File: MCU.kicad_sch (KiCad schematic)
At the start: 52 parts, among them J6 USB_C_Receptacle_USB2.0_16P, Q7 SI2301BDS, SW1 TS2306A, U16 W25Q128JVPIQ, U17 RP2354A, U4 TPD2E001DRLR, Y4 40MHz

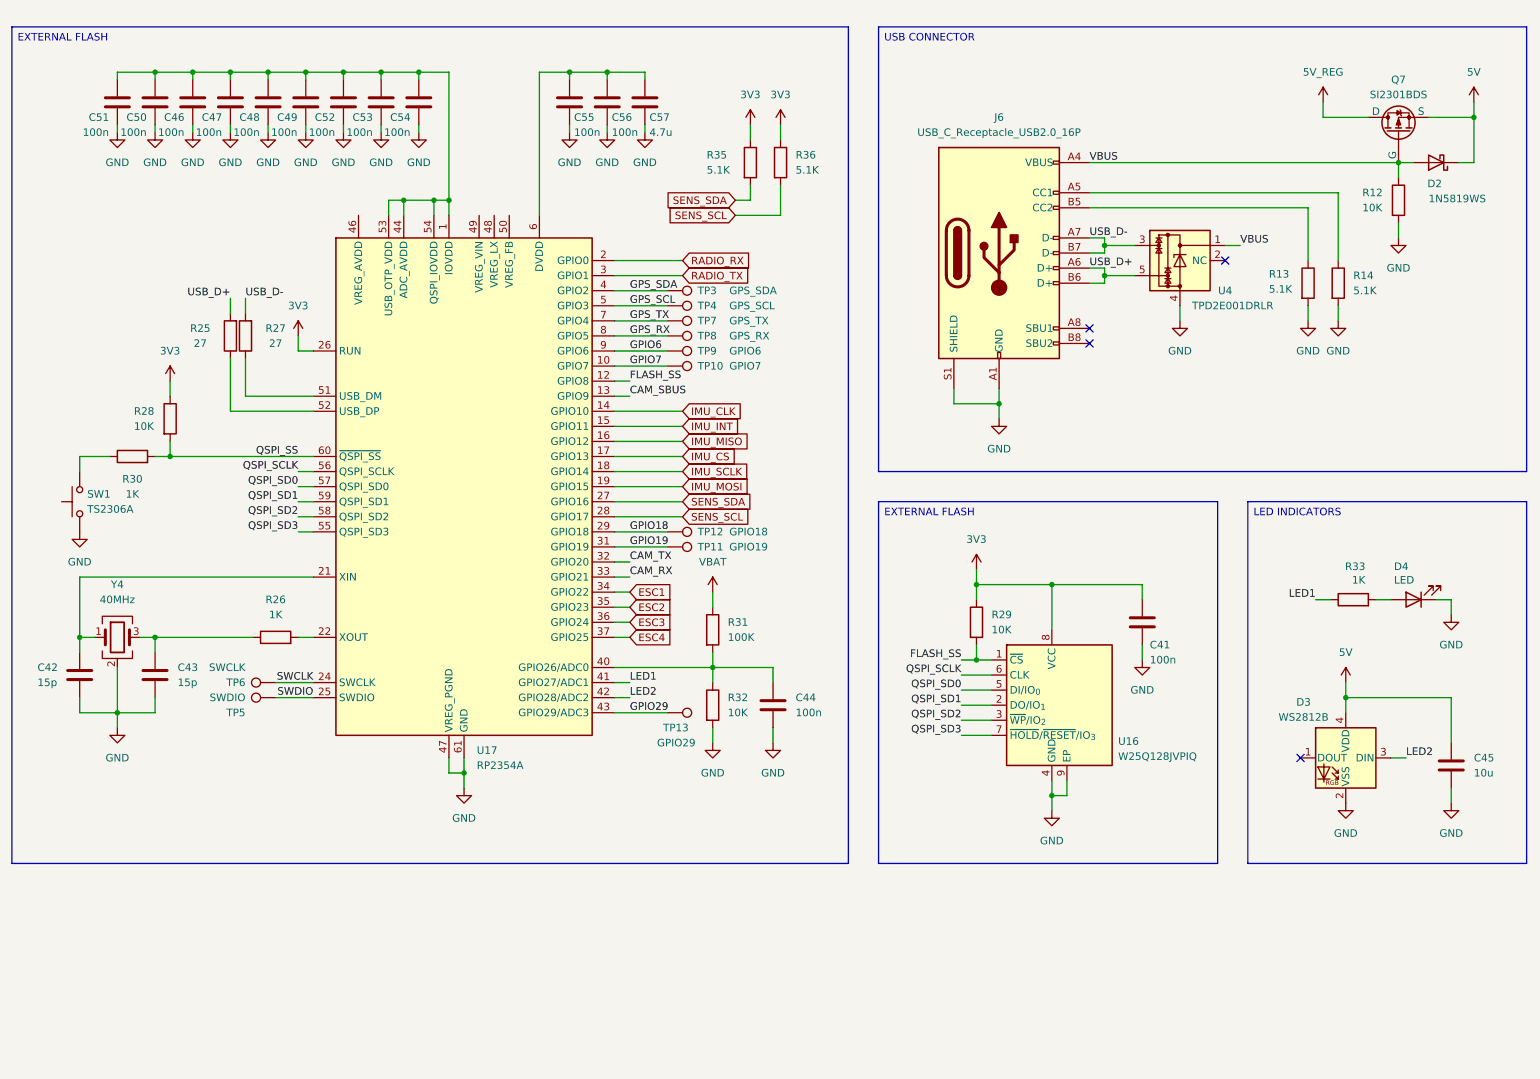
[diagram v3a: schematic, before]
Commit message: Complete ESC and MCU
Added the 4 ESC to the eschematic.
Updated the MCU design to add the connectors and buzzer.
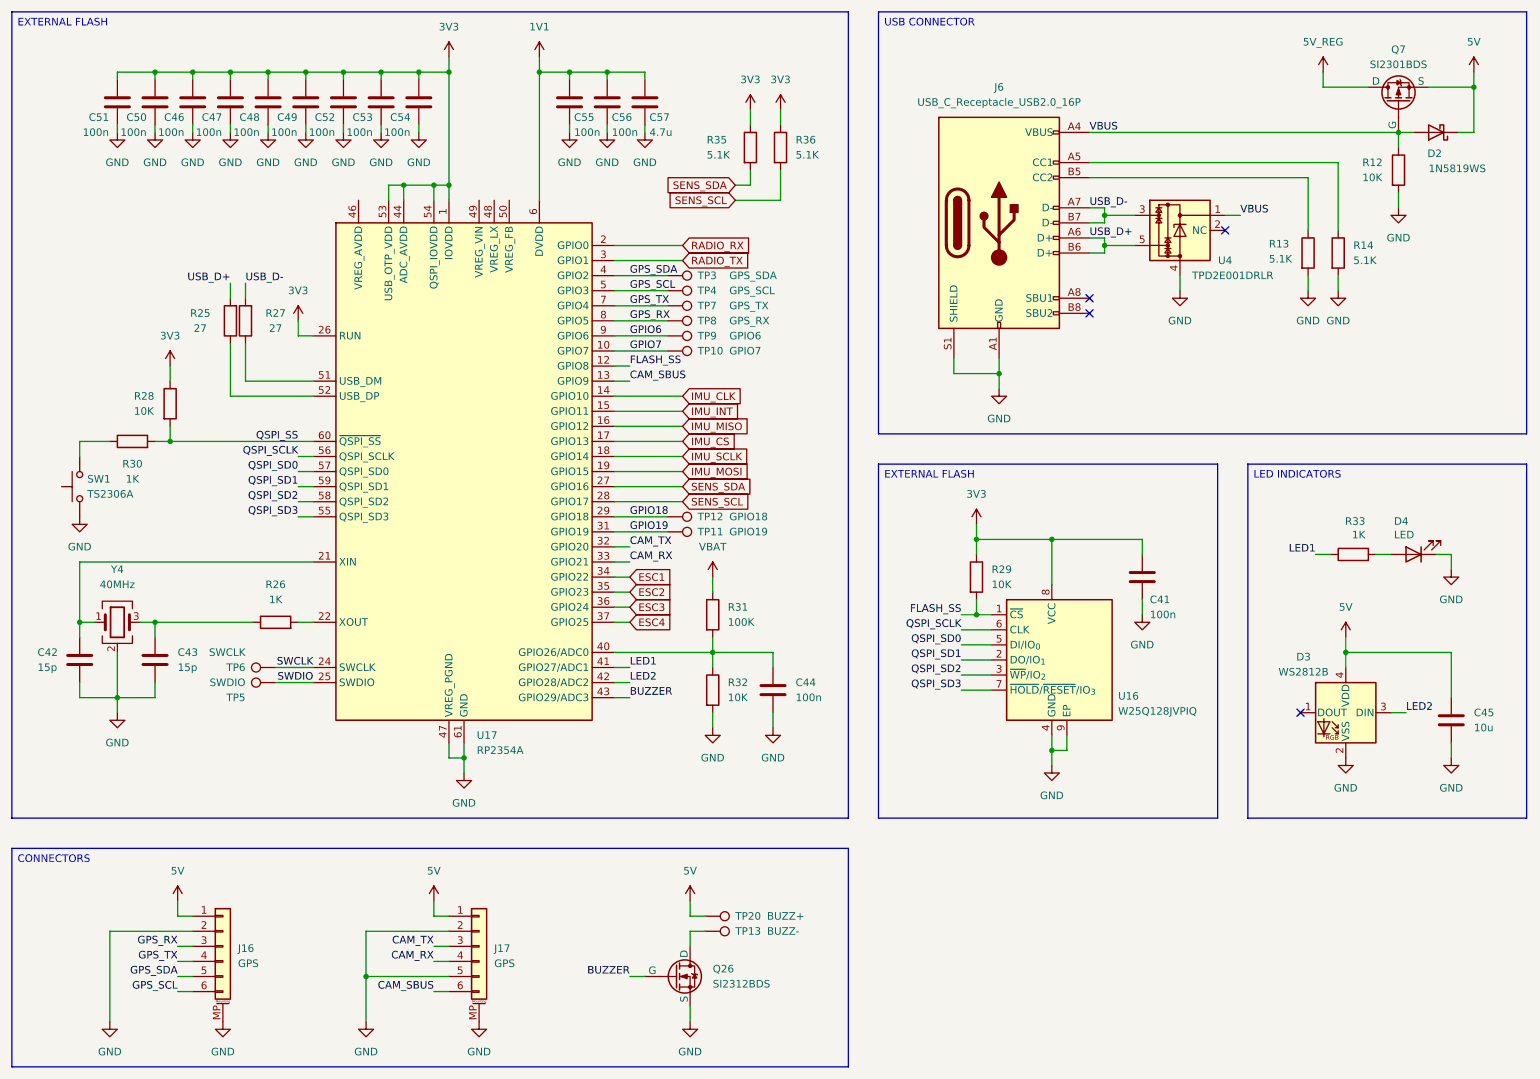
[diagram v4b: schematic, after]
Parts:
- added J16, J17: GPS, Connector_JST:JST_SH_SM06B-SRSS-TB_1x06-1MP_P1.00mm_Horizontal, symbol Connector_Generic_MountingPin:Conn_01x06_MountingPin
- added Q26: SI2312BDS, Package_TO_SOT_SMD:SOT-23, symbol Custom_Parts:SI2312BDS
- added TP20: BUZZ+, TestPoint:TestPoint_Pad_D1.0mm, symbol Connector:TestPoint
- TP13: value GPIO29 -> BUZZ-
- U17: footprint Package_DFN_QFN:QFN-60-1EP_7x7mm_P0.4mm_EP3.4x3.4mm -> Custom_Parts:RP2350A_QFN-60_EP_7.75x7.75_Pitch0.4mm
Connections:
- net 3V3: now also C46.1, C47.1, C48.1, C49.1, C50.1, C51.1, C52.1, C53.1, C54.1, U17.1 (IOVDD), U17.11 (IOVDD), U17.20 (IOVDD), U17.30 (IOVDD), U17.38 (IOVDD), U17.44 (ADC_AVDD), U17.45 (IOVDD), U17.53 (USB_OTP_VDD), U17.54 (QSPI_IOVDD)
- net 5V: now also J16.1 (Pin_1), J17.1 (Pin_1), TP20.1
- net CAM_RX: now also J17.4 (Pin_4)
- net CAM_SBUS: now also J17.6 (Pin_6)
- net CAM_TX: now also J17.3 (Pin_3)
- net GND: now also J16.2 (Pin_2), J16.MP (MountPin), J17.2 (Pin_2), J17.5 (Pin_5), J17.MP (MountPin), Q26.2 (S)
- net GPS_RX: now also J16.3 (Pin_3)
- net GPS_SCL: now also J16.6 (Pin_6)
- net GPS_SDA: now also J16.5 (Pin_5)
- net GPS_TX: now also J16.4 (Pin_4)
- net 1V1: now reaches C55.1, C56.1, C57.1, U17.23 (DVDD), U17.39 (DVDD), U17.6 (DVDD)
- net GPIO29: no longer names the net of TP13.1
- net GPIO29: now also Q26.3 (D); no longer U17.43 (GPIO29/ADC3)
- new net BUZZER: Q26.1 (G), U17.43 (GPIO29/ADC3)
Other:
- moved on the sheet: C41, C42, C43, C44, C45, D2, D3, D4, J6, Q7, R12, R13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

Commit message: Power design
Added the 5V regulator schematic.
Updated the MCU schematic.
Updated the RX schematic.
Updated the sensors schematic.

TODO:
Calculate the voltage divider for the 5V regulator.
Review all connections and systems.
Select the footprints for the missing components.
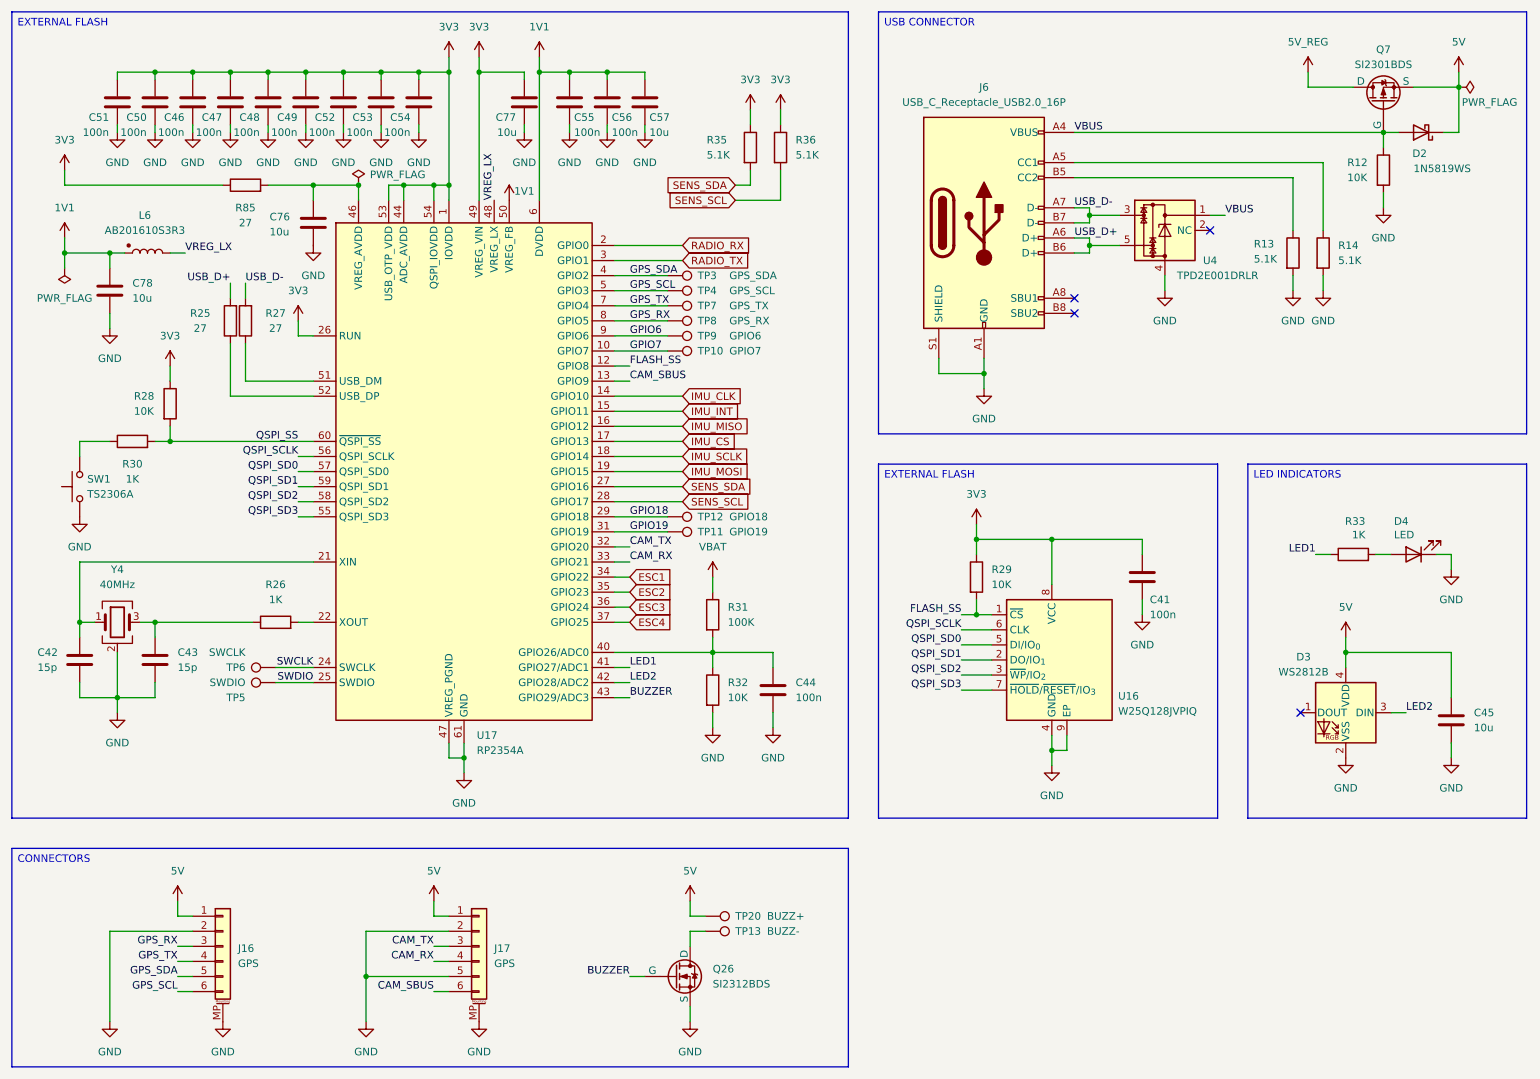
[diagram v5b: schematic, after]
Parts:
- added C76, C77, C78: 10u, symbol Device:C
- added L6: AB201610S3R3, symbol Custom_Parts:L_Polarized
- added R85: 27, symbol Device:R
- C57: value 4.7u -> 10u
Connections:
- net 1V1: now also U17.50 (VREG_FB), C78.1, L6.1
- net 3V3: now also U17.49 (VREG_VIN), C77.1, R85.1
- net GND: now also C76.2, C77.2, C78.2
- net at U17.46 (VREG_AVDD): now also C76.1, R85.2
- net VREG_LX: now reaches U17.48 (VREG_LX)
- net VREG_LX: now also L6.2
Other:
- moved on the sheet: D2, J6, Q7, R12, R13, R14, U4

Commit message: Footprints and revision
Added the missing footprints.
Updated a all the schematics.
Completed an initial review of the schematics.

TODO:
Perform a deep review of the schematics before committing to layout.
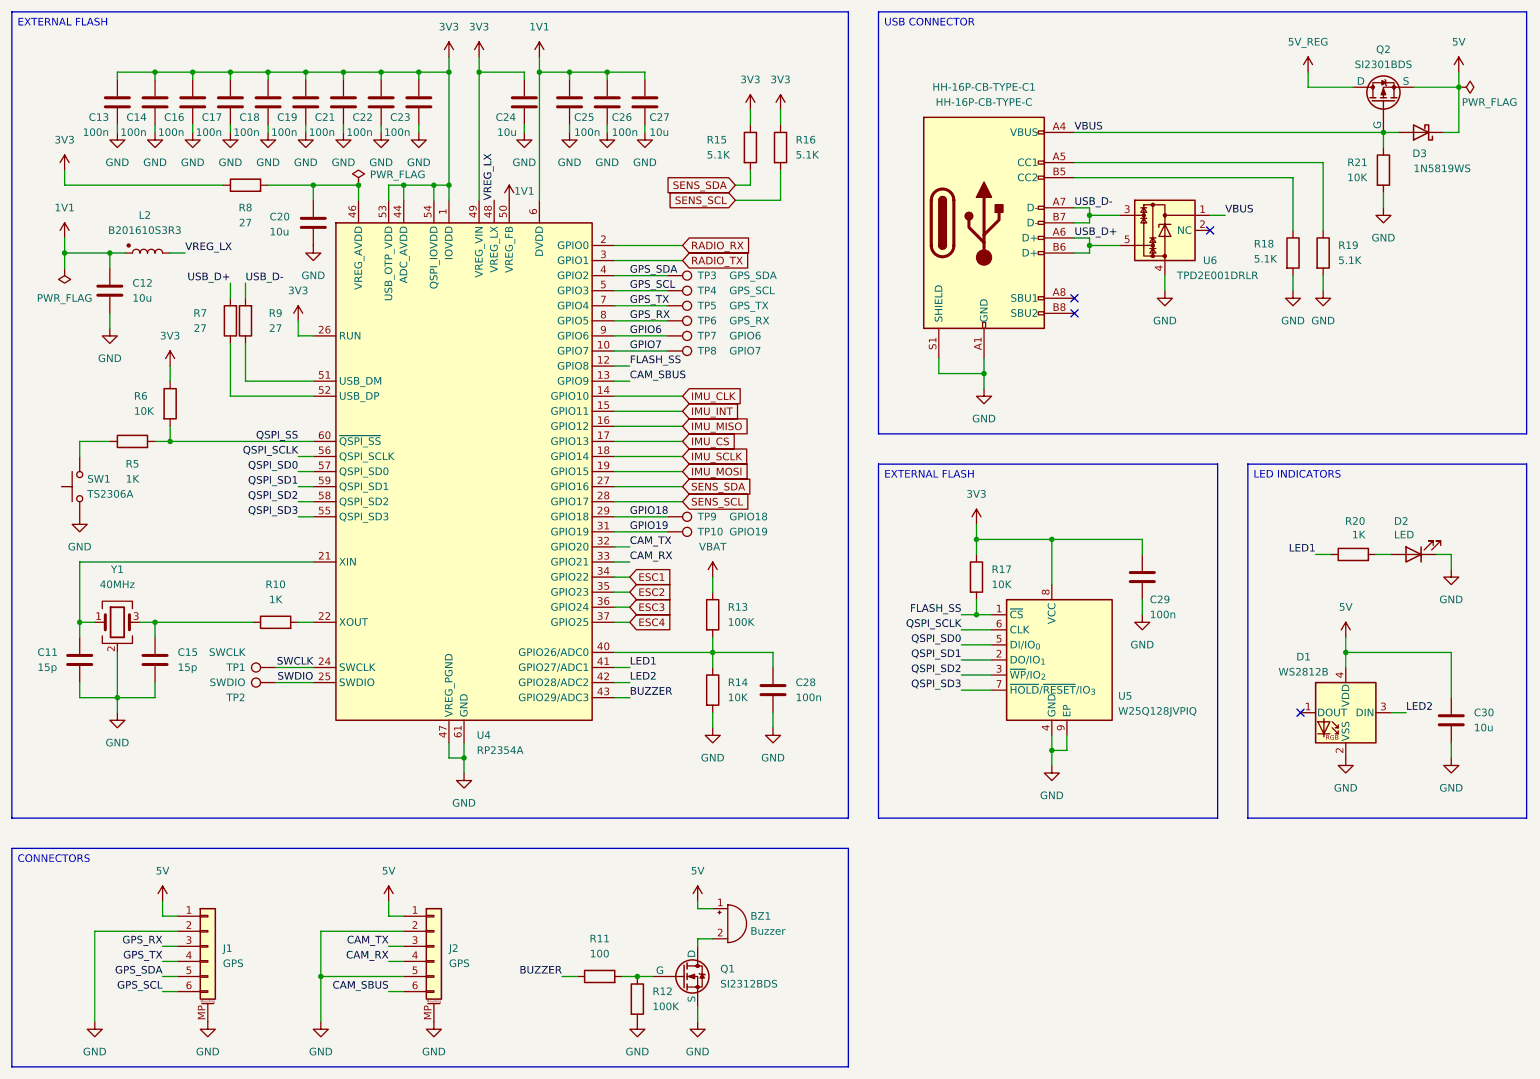
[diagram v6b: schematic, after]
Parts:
- removed J6: USB_C_Receptacle_USB2.0_16P, Custom_Parts:HH-16P-CB-TYPE-C, symbol Connector:USB_C_Receptacle_USB2.0_16P
- removed TP13: BUZZ-, TestPoint:TestPoint_Pad_D1.0mm, symbol Connector:TestPoint
- removed TP20: BUZZ+, TestPoint:TestPoint_Pad_D1.0mm, symbol Connector:TestPoint
- added BZ1: Buzzer, Custom_Parts:FUET_9018, symbol Device:Buzzer
- added HH-16P-CB-TYPE-C1: HH-16P-CB-TYPE-C, Custom_Parts:HH-16P-CB-TYPE-C, symbol Custom_Parts:HH-16P-CB-TYPE-C
- added R11: 100, Resistor_SMD:R_0603_1608Metric, symbol Device:R
- added R12: 100K, Resistor_SMD:R_0603_1608Metric, symbol Device:R
- C11: renamed from C42; footprint (none) -> Capacitor_SMD:C_0603_1608Metric
- C12: renamed from C78; footprint (none) -> Capacitor_SMD:C_0805_2012Metric
- C13: renamed from C51; footprint (none) -> Capacitor_SMD:C_0201_0603Metric
- C14: renamed from C50; footprint (none) -> Capacitor_SMD:C_0201_0603Metric
- C15: renamed from C43; footprint (none) -> Capacitor_SMD:C_0201_0603Metric
- C16: renamed from C46; footprint (none) -> Capacitor_SMD:C_0201_0603Metric
- C17: renamed from C47; footprint (none) -> Capacitor_SMD:C_0201_0603Metric
- C18: renamed from C48; footprint (none) -> Capacitor_SMD:C_0201_0603Metric
- C19: renamed from C49; footprint (none) -> Capacitor_SMD:C_0201_0603Metric
- C20: renamed from C76; footprint (none) -> Capacitor_SMD:C_0805_2012Metric
- C21: renamed from C52; footprint (none) -> Capacitor_SMD:C_0603_1608Metric
- C22: renamed from C53; footprint (none) -> Capacitor_SMD:C_0603_1608Metric
- C23: renamed from C54; footprint (none) -> Capacitor_SMD:C_0603_1608Metric
- C24: renamed from C77; footprint (none) -> Capacitor_SMD:C_0805_2012Metric
- C25: renamed from C55; footprint (none) -> Capacitor_SMD:C_0603_1608Metric
- C26: renamed from C56; footprint (none) -> Capacitor_SMD:C_0603_1608Metric
- C27: renamed from C57; footprint (none) -> Capacitor_SMD:C_0805_2012Metric
- C28: renamed from C44; footprint (none) -> Capacitor_SMD:C_0603_1608Metric
- C30: renamed from C45; footprint (none) -> Capacitor_SMD:C_0805_2012Metric
- L2: renamed from L6; value AB201610S3R3 -> B201610S3R3; footprint (none) -> Custom_Parts:AOTAB201610S3R3101T
- R10: renamed from R26; footprint (none) -> Resistor_SMD:R_0603_1608Metric
- R13: renamed from R31; footprint (none) -> Resistor_SMD:R_0603_1608Metric
- R14: renamed from R32; footprint (none) -> Resistor_SMD:R_0603_1608Metric
- R15: renamed from R35; footprint (none) -> Resistor_SMD:R_0603_1608Metric
- R16: renamed from R36; footprint (none) -> Resistor_SMD:R_0603_1608Metric
- R17: renamed from R29; footprint Resistor_SMD:R_0805_2012Metric -> Resistor_SMD:R_0603_1608Metric
- R18: renamed from R13; footprint (none) -> Resistor_SMD:R_0603_1608Metric
- R19: renamed from R14; footprint (none) -> Resistor_SMD:R_0603_1608Metric
- R20: renamed from R33; footprint Resistor_SMD:R_0805_2012Metric -> Resistor_SMD:R_0603_1608Metric
- R21: renamed from R12; footprint (none) -> Resistor_SMD:R_0603_1608Metric
- R5: renamed from R30; footprint (none) -> Resistor_SMD:R_0603_1608Metric
- R6: renamed from R28; footprint (none) -> Resistor_SMD:R_0603_1608Metric
- R7: renamed from R25; footprint (none) -> Resistor_SMD:R_0603_1608Metric
- R8: renamed from R85; footprint (none) -> Resistor_SMD:R_0603_1608Metric
- R9: renamed from R27; footprint (none) -> Resistor_SMD:R_0603_1608Metric
- renumbered C41 to C29, D3 to D1, D4 to D2, D2 to D3, J16 to J1, J17 to J2, Q26 to Q1, Q7 to Q2, TP6 to TP1, TP11 to TP10, TP5 to TP2, TP7 to TP5, TP8 to TP6, TP9 to TP7, TP10 to TP8, TP12 to TP9, U17 to U4, U16 to U5, U4 to U6, Y4 to Y1
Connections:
- net 5V: now also BZ1.1 (+)
- net BUZZER: now also R11.1; no longer Q1.1 (G)
- net GND: now also HH-16P-CB-TYPE-C1.A1 (GND), HH-16P-CB-TYPE-C1.B1 (GND), HH-16P-CB-TYPE-C1.S1 (SHIELD), R12.2
- net USB_D+: now also HH-16P-CB-TYPE-C1.A6 (D+), HH-16P-CB-TYPE-C1.B6 (D+)
- net USB_D-: now also HH-16P-CB-TYPE-C1.A7 (D-), HH-16P-CB-TYPE-C1.B7 (D-)
- net VBUS: now also HH-16P-CB-TYPE-C1.A4 (VBUS), HH-16P-CB-TYPE-C1.B4 (VBUS)
- net at R19.1: now also HH-16P-CB-TYPE-C1.A5 (CC1)
- net at R18.1: now also HH-16P-CB-TYPE-C1.B5 (CC2)
- net at Q1.3 (D): now also BZ1.2 (-)
- new net: Q1.1 (G), R11.2, R12.1
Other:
- moved on the sheet: J1, J2, Q1
